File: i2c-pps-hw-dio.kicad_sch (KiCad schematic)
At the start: 0 parts

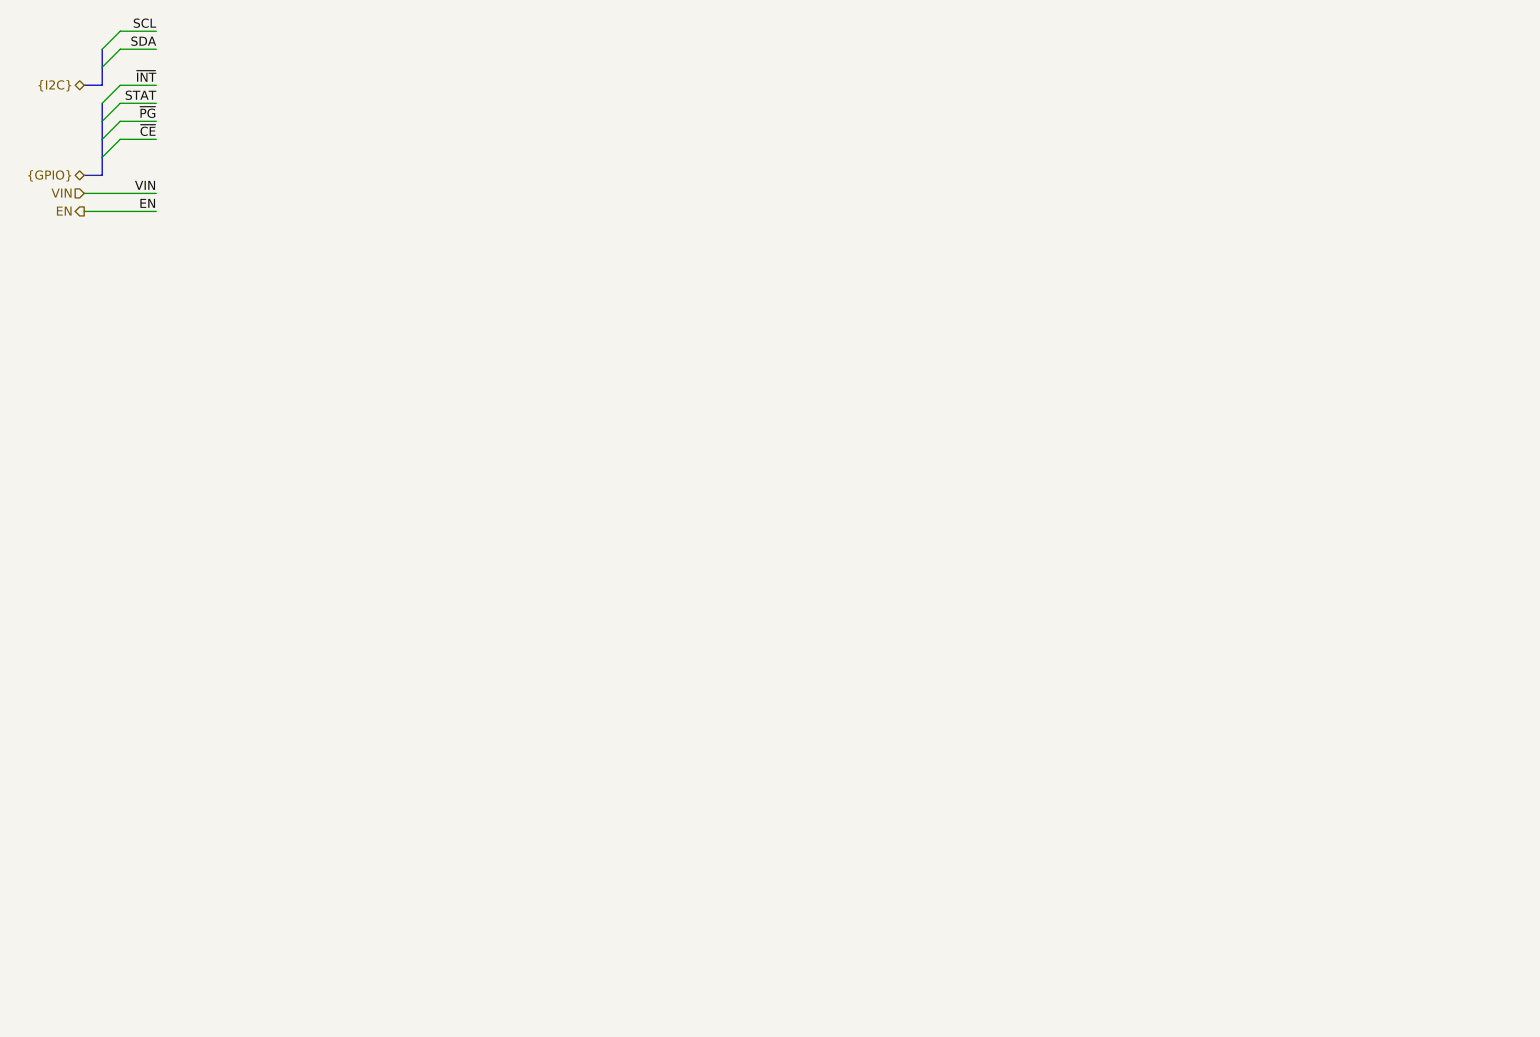
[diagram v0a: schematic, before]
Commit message: Design schematics and set per component requirements
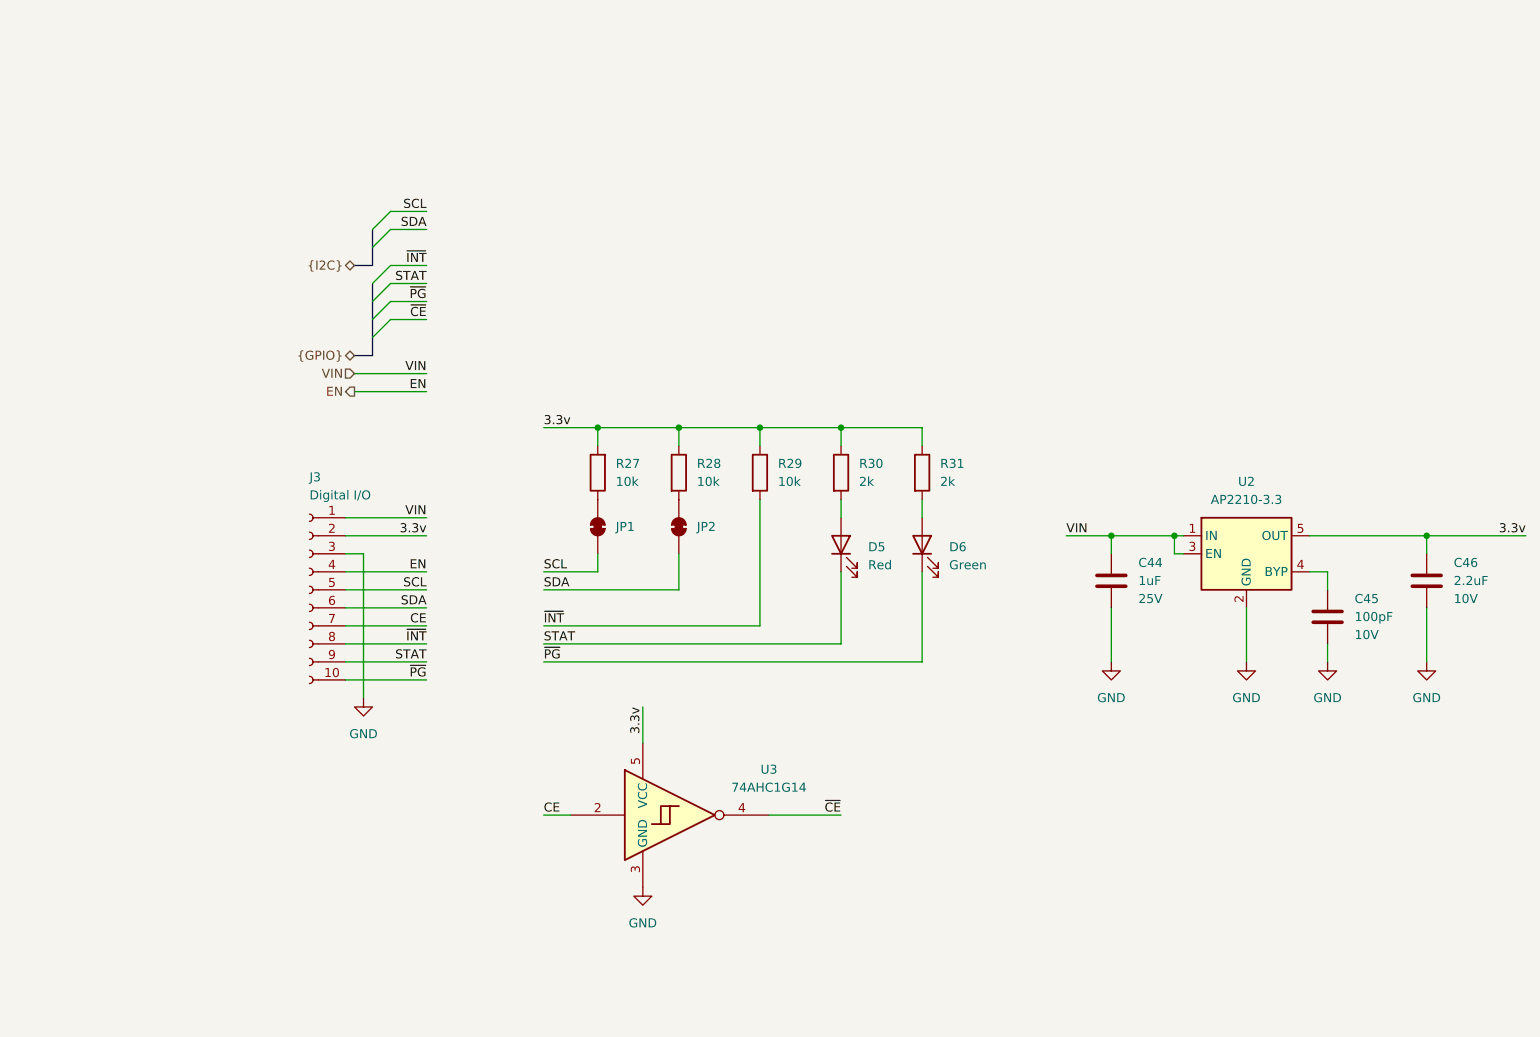
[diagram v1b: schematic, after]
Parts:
- added C44: 1uF, Capacitor_SMD:C_0805_2012Metric, symbol Device:C
- added C45: 100pF, Capacitor_SMD:C_0603_1608Metric_Pad1.08x0.95mm_HandSolder, symbol Device:C
- added C46: 2.2uF, Capacitor_SMD:C_0805_2012Metric, symbol Device:C
- added D5: Red, LED_SMD:LED_0603_1608Metric_Pad1.05x0.95mm_HandSolder, symbol Device:LED
- added D6: Green, LED_SMD:LED_0603_1608Metric_Pad1.05x0.95mm_HandSolder, symbol Device:LED
- added J3: Digital I/O, symbol Connector:Conn_01x10_Socket
- added JP1, JP2: ~, symbol Jumper:SolderJumper_2_Bridged
- added R27, R28, R29: 10k, Resistor_SMD:R_0603_1608Metric_Pad0.98x0.95mm_HandSolder, symbol Device:R
- added R30, R31: 2k, Resistor_SMD:R_0603_1608Metric_Pad0.98x0.95mm_HandSolder, symbol Device:R
- added U2: AP2210-3.3, Package_TO_SOT_SMD:SOT-23-5, symbol i2c-pps-hw:AP2210-3.3
- added U3: 74AHC1G14, symbol 74xGxx:74AHC1G14
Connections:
- net EN: now also J3.4 (Pin_4)
- net SCL: now also J3.5 (Pin_5), JP1.1 (A)
- net SDA: now also J3.6 (Pin_6), JP2.1 (A)
- net STAT: now also D5.1 (K), J3.9 (Pin_9)
- net VIN: now also C44.1, J3.1 (Pin_1), U2.1 (IN), U2.3 (EN)
- net ~{CE}: now also U3.4
- net ~{INT}: now also J3.8 (Pin_8), R29.2
- net ~{PG}: now also D6.1 (K), J3.10 (Pin_10)
- new net: C45.1, U2.4 (BYP)
- new net: JP1.2 (B), R27.1
- new net: D6.2 (A), R31.2
- new net: JP2.2 (B), R28.2
- new net: D5.2 (A), R30.2
- new net 3.3v: C46.1, J3.2 (Pin_2), R27.2, R28.1, R29.1, R30.1, R31.1, U2.5 (OUT), U3.5 (VCC)
- new net CE: J3.7 (Pin_7), U3.2
- new net GND: C44.2, C45.2, C46.2, J3.3 (Pin_3), U2.2 (GND), U3.3 (GND)

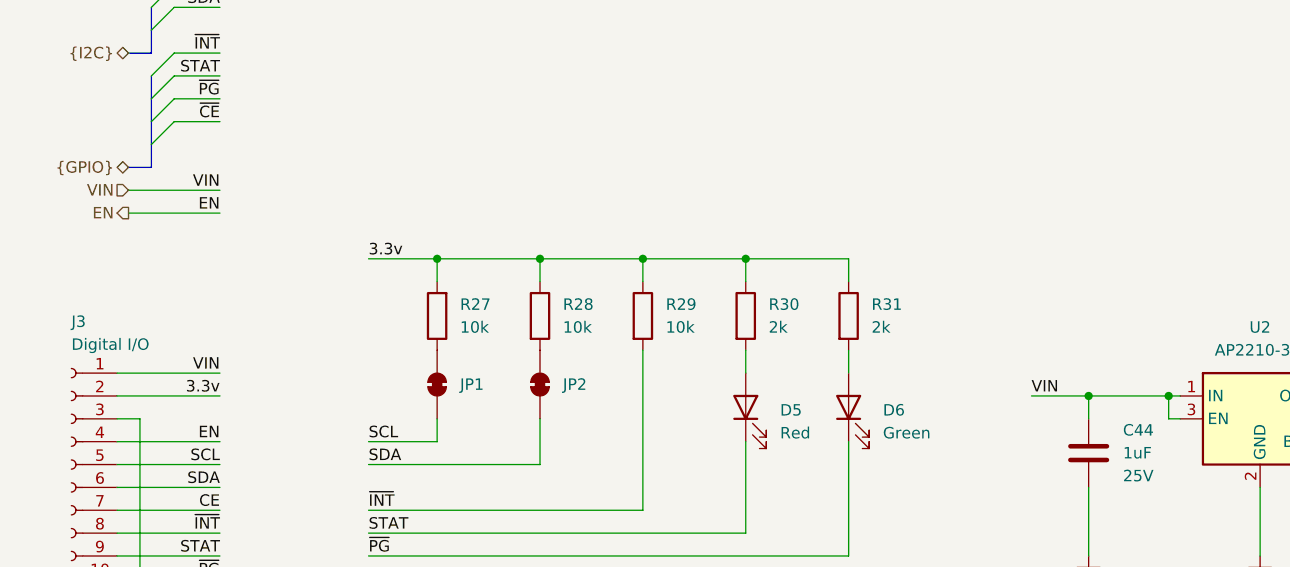
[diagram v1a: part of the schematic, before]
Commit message: Rename VIN to +5V_Prot for clarity
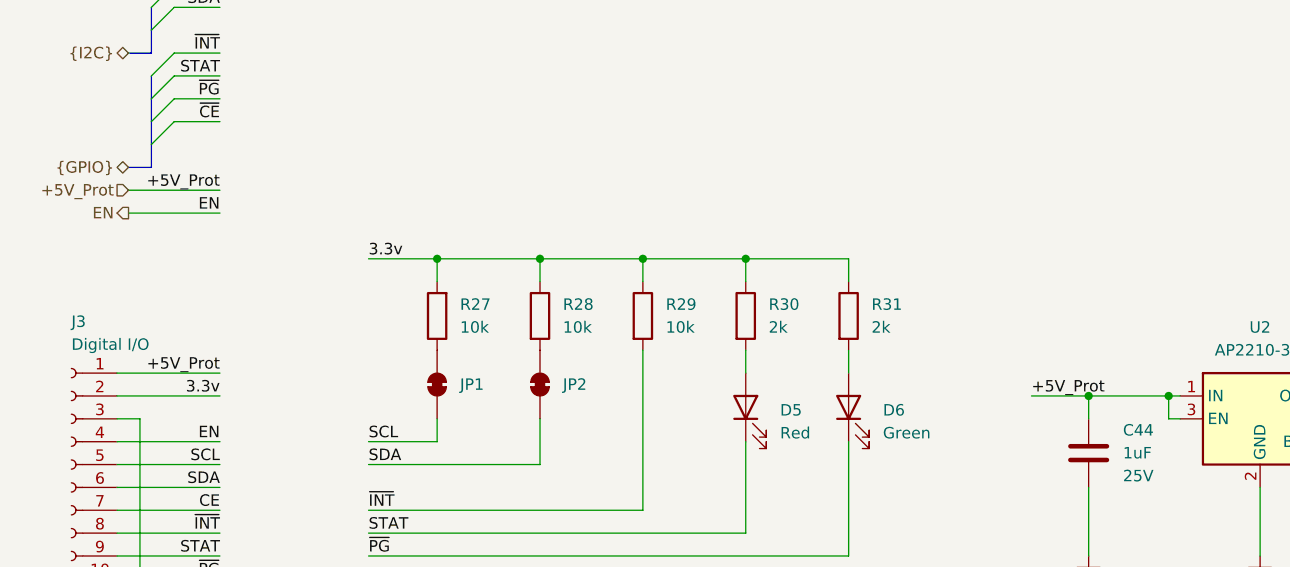
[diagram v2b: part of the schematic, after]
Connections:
- net at U2.4 (BYP): now also C45.1
- net VIN renamed +5V_Prot
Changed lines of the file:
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@@
 		)
 	)
-	(label "VIN"
+	(label "+5V_Prot"
 		(at 73.66 93.98 180)
 		(effects
@@
 		)
 	)
-	(label "VIN"
+	(label "+5V_Prot"
 		(at 73.66 73.66 180)
 		(effects
@@
 		)
 	)
-	(label "VIN"
+	(label "+5V_Prot"
 		(at 163.83 96.52 0)
 		(effects
@@
 		)
 	)
-	(hierarchical_label "VIN"
+	(hierarchical_label "+5V_Prot"
 		(shape input)
 		(at 63.5 73.66 180)

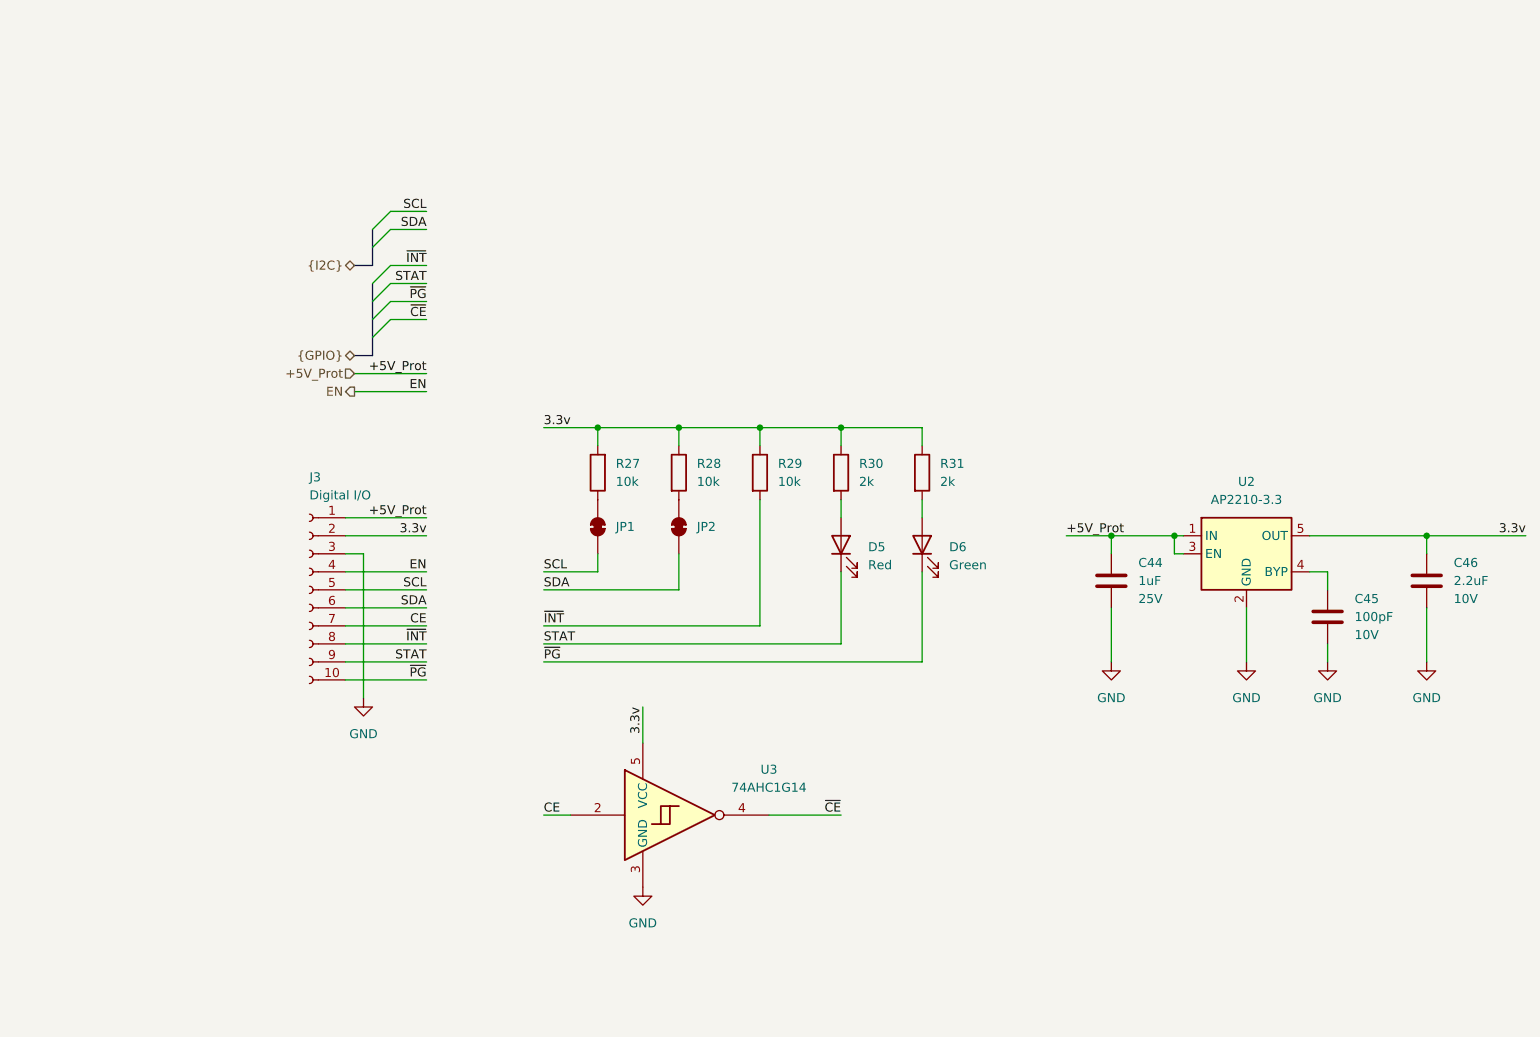
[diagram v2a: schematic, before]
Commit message: Add more indicator LEDs
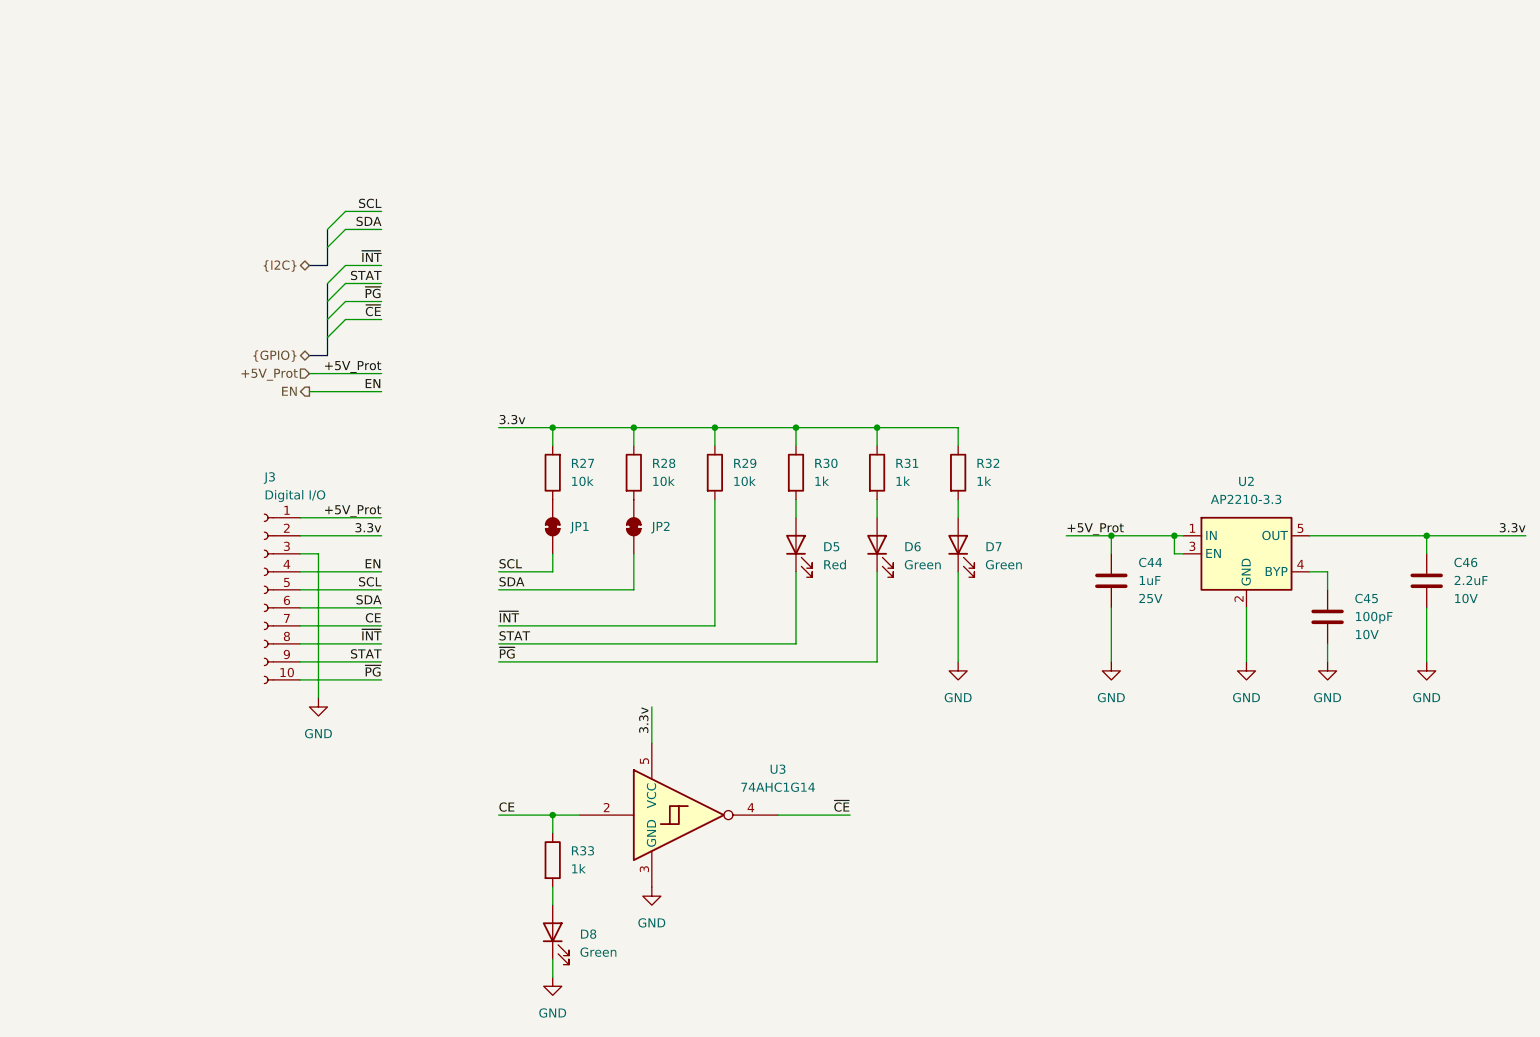
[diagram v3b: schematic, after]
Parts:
- added D7, D8: Green, LED_SMD:LED_0603_1608Metric_Pad1.05x0.95mm_HandSolder, symbol Device:LED
- added R32, R33: 1k, Resistor_SMD:R_0603_1608Metric_Pad0.98x0.95mm_HandSolder, symbol Device:R
- R30, R31: value 2k -> 1k
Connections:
- net 3.3v: now also R32.1
- net CE: now also R33.1
- net GND: now also D7.1 (K), D8.1 (K)
- net at U2.4 (BYP): now also C45.1
- new net: D7.2 (A), R32.2
- new net: D8.2 (A), R33.2
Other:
- moved on the sheet: D5, D6, J3, JP1, JP2, R27, R28, R29, R30, R31, U3

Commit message: Fix errors and warnings reported by ERC
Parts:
- U2: Manufacturer (none) -> Diodes Incorporated
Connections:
- net at U2.4 (BYP): now also C45.1
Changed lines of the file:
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@@
 			)
 		)
-		(property "Datasheet" "http://www.ti.com/lit/ds/symlink/lp5907.pdf"
+		(property "Datasheet" "https://www.diodes.com/assets/Datasheets/AP2210.pdf"
 			(at 189.23 86.36 0)
 			(effects
@@
 			)
 		)
+		(property "Manufacturer" "Diodes Incorporated"
+			(at 189.23 99.06 0)
+			(effects
+				(font
+					(size 1.27 1.27)
+				)
+				(hide yes)
+			)
+		)
 		(pin "1"
 		)
@@
 		)
 		(pin "4"
-		)
-		(pin "4"

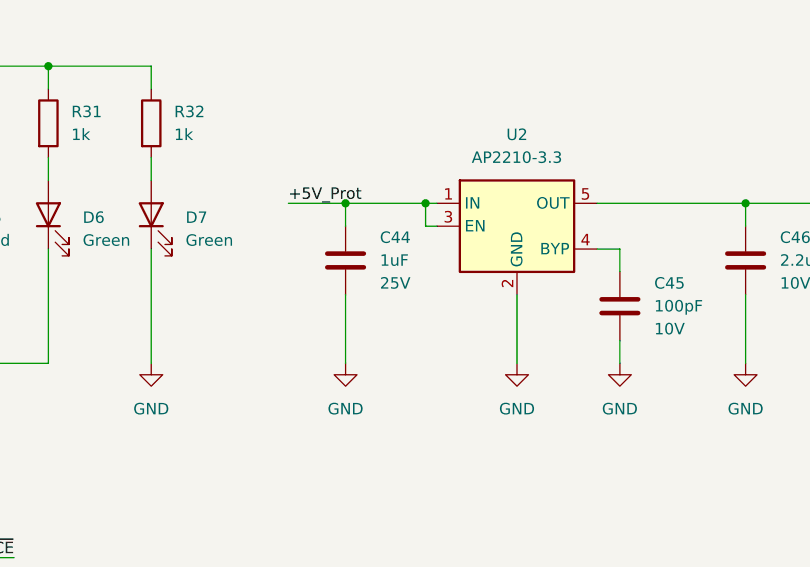
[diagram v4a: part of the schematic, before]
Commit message: Select market available components
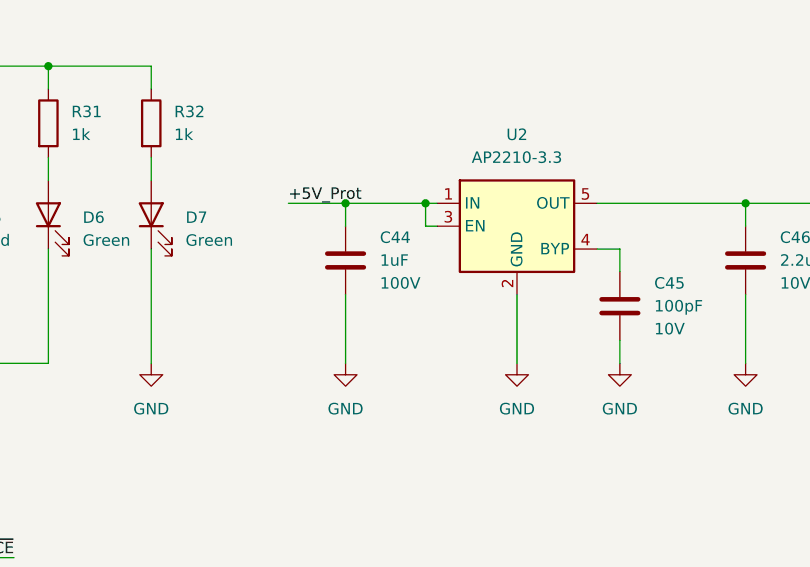
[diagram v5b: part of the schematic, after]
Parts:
- C44: Manufacturer (none) -> KYOCERA AVX; Part Number (none) -> 08051C105K4Z2A; Rated Voltage 25V -> 100V
- C45: Manufacturer (none) -> Würth Elektronik; Part Number (none) -> 885012206003
- C46: footprint Capacitor_SMD:C_0805_2012Metric -> Capacitor_SMD:C_0603_1608Metric_Pad1.08x0.95mm_HandSolder; Manufacturer (none) -> Murata Electronics; Part Number (none) -> GRM188R71A225KE15J
- D5: Manufacturer (none) -> Lite-On Inc; Part Number (none) -> LTST-C193KRKT-2A
- D6, D7, D8: Manufacturer (none) -> Lite-On Inc; Part Number (none) -> LTST-C190GKT
- J3: footprint (none) -> Connector_PinSocket_2.54mm:PinSocket_2x05_P2.54mm_Vertical; Manufacturer (none) -> Sullins Connector Solutions; Part Number (none) -> PPPC052LFBN-RC
- JP1, JP2: footprint (none) -> i2c-pps-hw:SolderJumper-2_P0.65mm_Bridged_RoundedPad0.5x0.75mm
- R27, R28, R29: Manufacturer (none) -> YAGEO; Part Number (none) -> RC0603JR-0710KL
- R30, R31, R32, R33: Manufacturer (none) -> YAGEO; Part Number (none) -> RC0603JR-071KL
- U2: Part Number (none) -> AP2210N-3.3TRG1
- U3: footprint (none) -> Package_TO_SOT_SMD:SOT-23-5_HandSoldering; Manufacturer (none) -> Texas Instruments; Part Number (none) -> SN74AHC1G14DBVR
